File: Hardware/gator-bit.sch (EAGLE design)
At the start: 92 parts, among them J1 GATOR, J10 GATOR, J11 GATOR, J12 GATOR, J13 GATOR, J14 GATOR, J15 GATOR, J16 GATOR, J17 GATOR, J18 GATOR, J2 GATOR, J3 GATOR, J4 GATOR, J6 GATOR, J7 GATOR, J8 GATOR, J9 GATOR, U1 TPS63070, U2 micro:bit, U3 TXB0104, U4 ADJ REG 1.5A

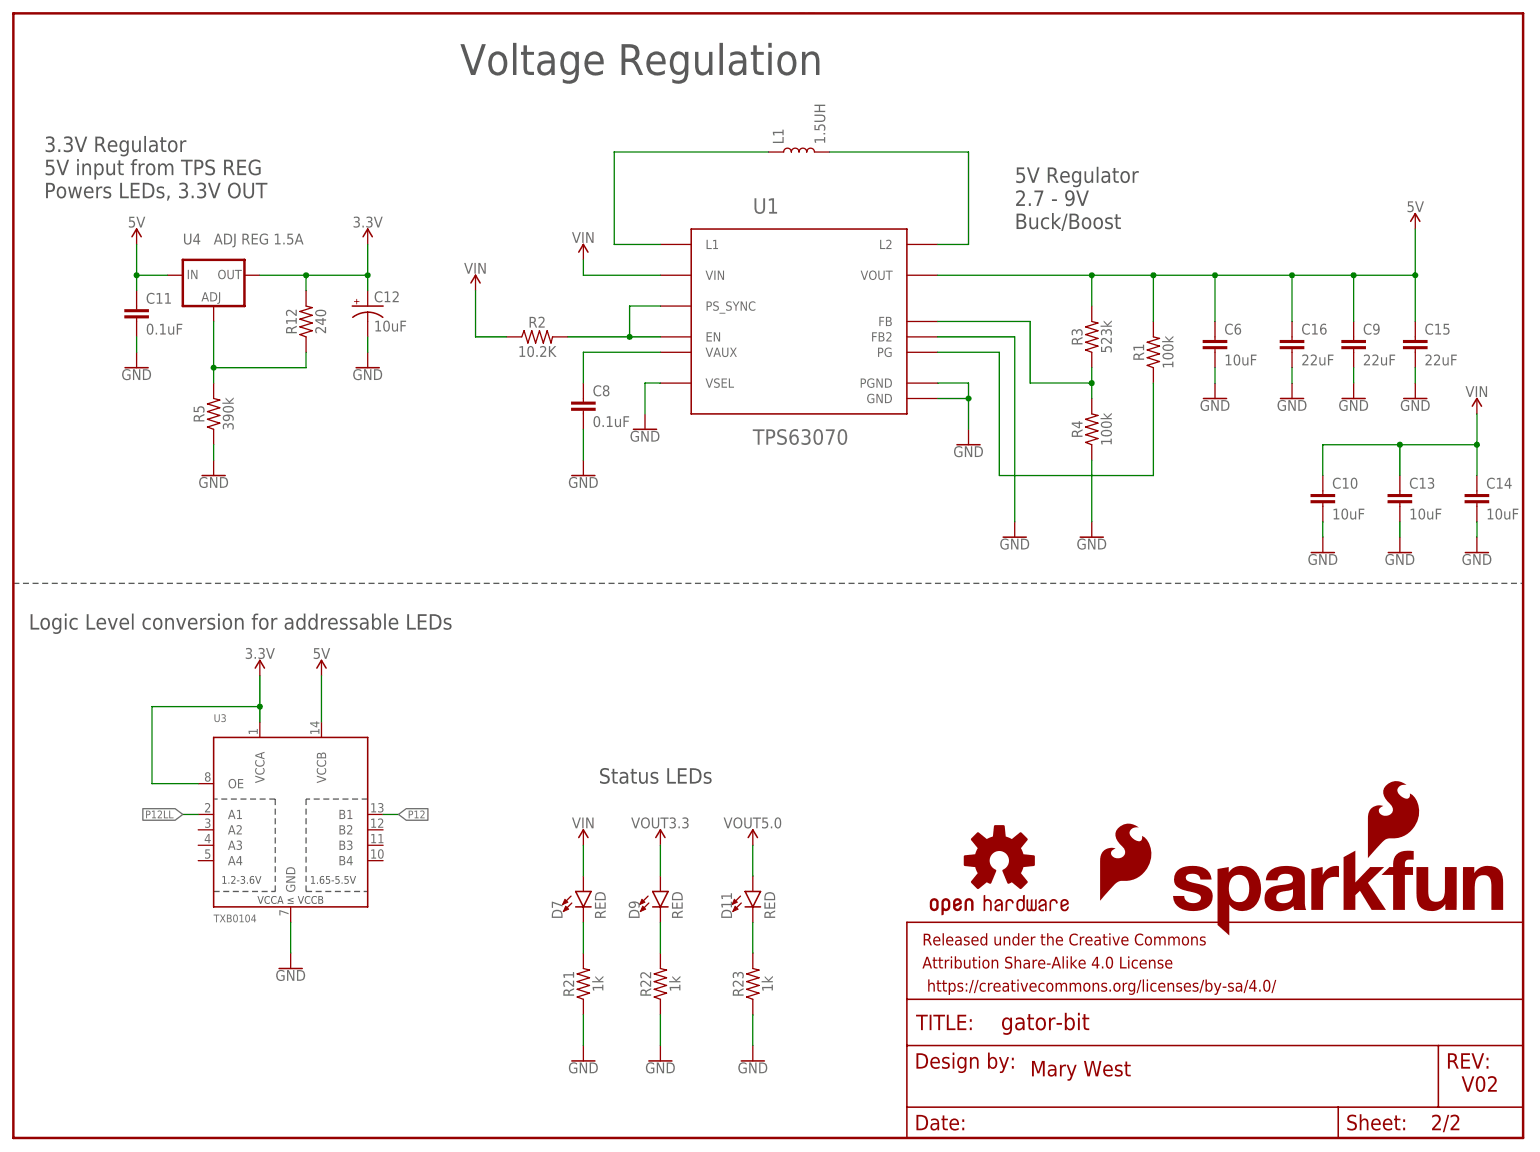
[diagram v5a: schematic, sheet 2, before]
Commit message: Updating TXB package
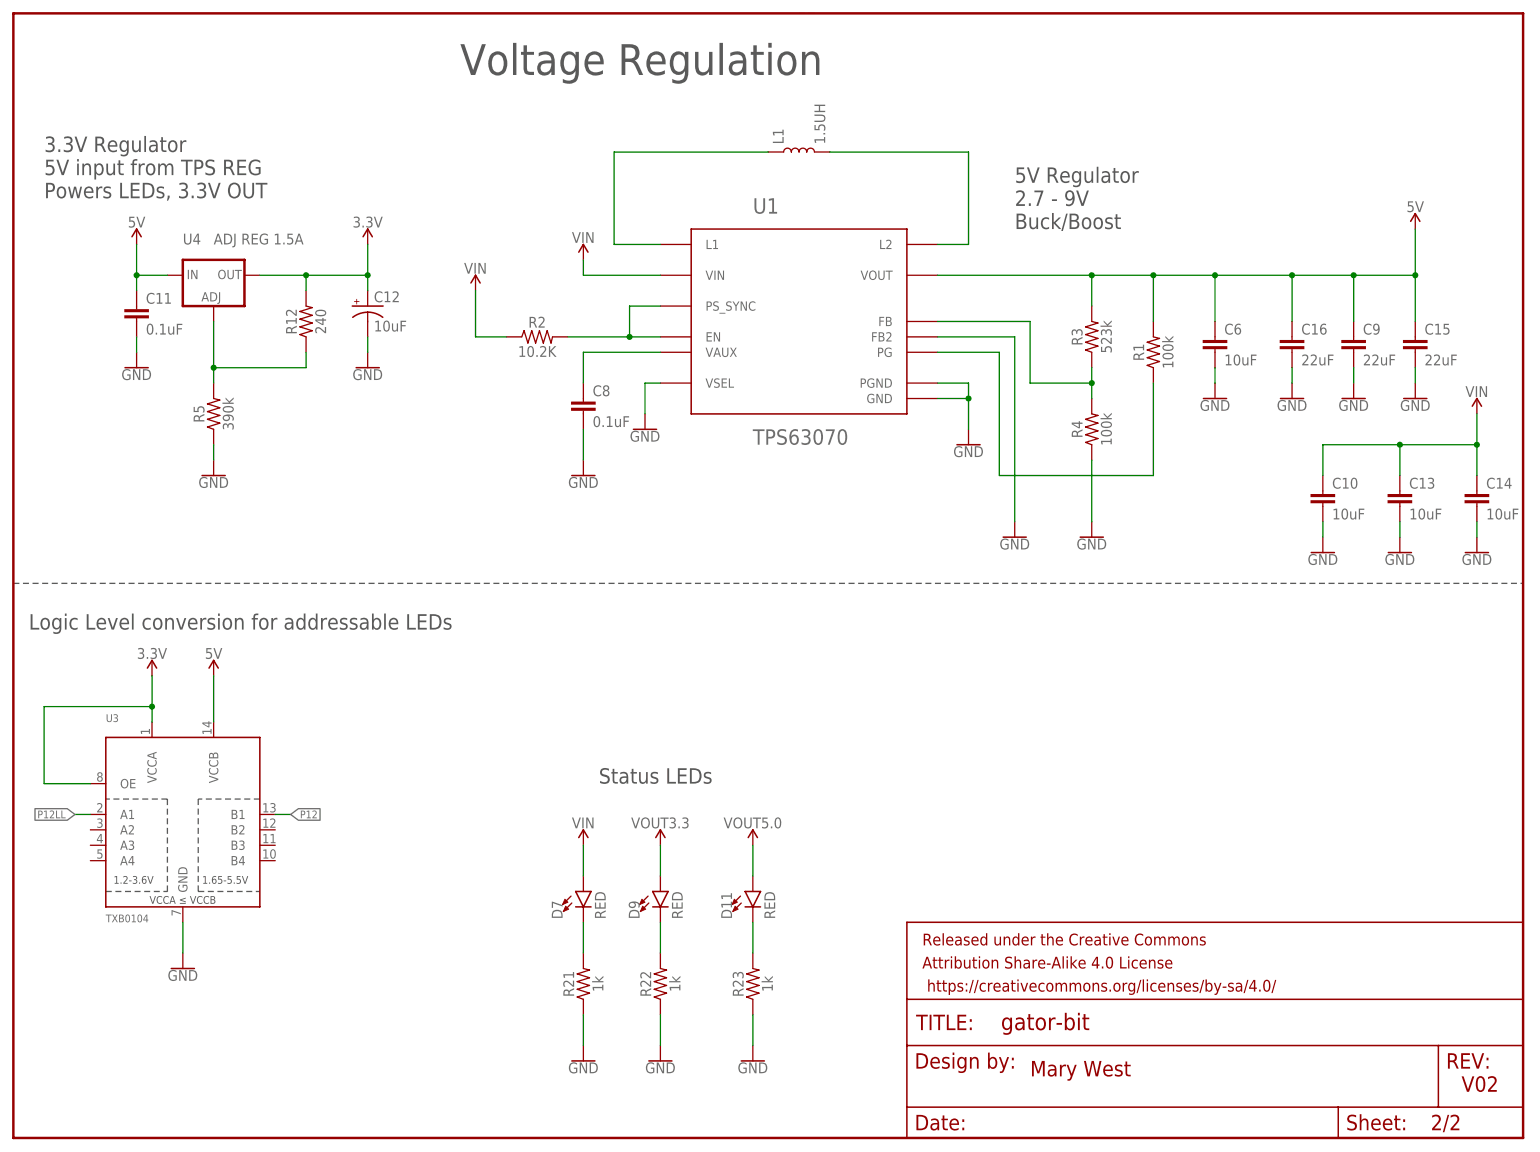
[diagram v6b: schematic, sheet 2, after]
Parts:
- removed LOGO4: SFE_LOGO_NAME_FLAME.3_INCH, SparkFun-Aesthetics:SFE_LOGO_NAME_FLAME.3_INCH
- removed LOGO5: SFE_LOGO_FLAME.3_INCH, SparkFun-Aesthetics:SFE_LOGO_FLAME.3_INCH
- removed LOGO6: OSHW-LOGOL, SparkFun-Aesthetics:OSHW-LOGOL
- added LOGO1: SFE_LOGO_NAME_FLAME.3_INCH, SparkFun-Aesthetics:SFE_LOGO_NAME_FLAME.3_INCH
- added LOGO2: OSHW-LOGOM, SparkFun-Aesthetics:OSHW-LOGOM
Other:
- moved on the sheet: U3
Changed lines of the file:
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@@
 <?xml version="1.0" encoding="utf-8"?>
 <!DOCTYPE eagle SYSTEM "eagle.dtd">
-<eagle version="8.5.1">
+<eagle version="7.7.0">
 <drawing>
 <settings>
 <setting alwaysvectorfont="no"/>
-<setting keepoldvectorfont="yes"/>
 <setting verticaltext="up"/>
 </settings>
@@
 <part name="S2" library="SparkFun-Switches" deviceset="SWITCH-SPDT" device="-SMD-AYZ0202"/>
 <part name="D6" library="SparkFun-DiscreteSemi" deviceset="DIODE-SCHOTTKY" device="-BAT20J" value="1A/23V/620mV"/>
-<part name="LOGO4" library="SparkFun-Aesthetics" deviceset="SFE_LOGO_NAME_FLAME" device=".3_INCH"/>
-<part name="LOGO5" library="SparkFun-Aesthetics" deviceset="SFE_LOGO_FLAME" device=".3_INCH" value="SFE_LOGO_FLAME.3_INCH"/>
-<part name="LOGO6" library="SparkFun-Aesthetics" deviceset="OSHW-LOGO" device="L"/>
 <part name="SUPPLY1" library="SparkFun-PowerSymbols" deviceset="5V" device=""/>
 <part name="C10" library="SparkFun-Capacitors" deviceset="10UF" device="-0805-10V-10%" value="10uF"/>
@@
 <part name="F1" library="SparkFun-Fuses" deviceset="PPTC" device="_HALF-AMP" value="6V/0.5A"/>
 <part name="SUPPLY3" library="SparkFun-PowerSymbols" deviceset="3.3V" device=""/>
+<part name="LOGO1" library="SparkFun-Aesthetics" deviceset="SFE_LOGO_NAME_FLAME" device=".3_INCH" value="SFE_LOGO_NAME_FLAME.3_INCH"/>
+<part name="LOGO2" library="SparkFun-Aesthetics" deviceset="OSHW-LOGO" device="M" value="OSHW-LOGOM"/>
 </parts>
 <sheets>
@@
 </instance>
 <instance part="SUPPLY3" gate="G$1" x="68.58" y="172.72"/>
+<instance part="LOGO1" gate="G$1" x="193.04" y="33.02"/>
+<instance part="LOGO2" gate="G$1" x="172.72" y="45.72"/>
 </instances>
 <busses>
@@
 <instance part="R12" gate="G$1" x="48.26" y="134.62" rot="R90"/>
 <instance part="GND28" gate="1" x="33.02" y="109.22"/>
-<instance part="LOGO4" gate="G$1" x="190.5" y="33.02"/>
-<instance part="LOGO5" gate="G$1" x="178.816" y="38.608"/>
-<instance part="LOGO6" gate="G$1" x="162.56" y="45.72"/>
 <instance part="C10" gate="G$1" x="215.9" y="104.14"/>
 <instance part="C13" gate="G$1" x="228.6" y="104.14"/>
@@
 <instance part="GND30" gate="1" x="215.9" y="96.52"/>
 <instance part="SUPPLY5" gate="G$1" x="241.3" y="119.38"/>
-<instance part="U3" gate="G$1" x="45.72" y="50.8"/>
-<instance part="SUPPLY7" gate="G$1" x="40.64" y="76.2"/>
-<instance part="SUPPLY8" gate="G$1" x="50.8" y="76.2"/>
-<instance part="GND31" gate="1" x="45.72" y="27.94"/>
+<instance part="U3" gate="G$1" x="27.94" y="50.8"/>
+<instance part="SUPPLY7" gate="G$1" x="22.86" y="76.2"/>
+<instance part="SUPPLY8" gate="G$1" x="33.02" y="76.2"/>
+<instance part="GND31" gate="1" x="27.94" y="27.94"/>
 <instance part="D7" gate="G$1" x="93.98" y="40.64"/>
 <instance part="D9" gate="G$1" x="106.68" y="40.64"/>
@@
 <segment>
 <pinref part="U3" gate="G$1" pin="GND"/>
-<wire x1="45.72" y1="35.56" x2="45.72" y2="30.48" width="0.1524" layer="91"/>
+<wire x1="27.94" y1="35.56" x2="27.94" y2="30.48" width="0.1524" layer="91"/>
 <pinref part="GND31" gate="1" pin="GND"/>
 </segment>
@@
 <segment>
 <pinref part="U3" gate="G$1" pin="VCCB"/>
-<wire x1="50.8" y1="68.58" x2="50.8" y2="76.2" width="0.1524" layer="91"/>
+<wire x1="33.02" y1="68.58" x2="33.02" y2="76.2" width="0.1524" layer="91"/>
 <pinref part="SUPPLY8" gate="G$1" pin="5V"/>
 </segment>
@@
 <segment>
 <pinref part="U3" gate="G$1" pin="VCCA"/>
-<wire x1="40.64" y1="68.58" x2="40.64" y2="71.12" width="0.1524" layer="91"/>
+<wire x1="22.86" y1="68.58" x2="22.86" y2="71.12" width="0.1524" layer="91"/>
 <pinref part="SUPPLY7" gate="G$1" pin="3.3V"/>
 <pinref part="U3" gate="G$1" pin="OE"/>
-<wire x1="40.64" y1="71.12" x2="40.64" y2="76.2" width="0.1524" layer="91"/>
-<wire x1="30.48" y1="58.42" x2="22.86" y2="58.42" width="0.1524" layer="91"/>
-<wire x1="22.86" y1="58.42" x2="22.86" y2="71.12" width="0.1524" layer="91"/>
-<wire x1="22.86" y1="71.12" x2="40.64" y2="71.12" width="0.1524" layer="91"/>
-<junction x="40.64" y="71.12"/>
+<wire x1="22.86" y1="71.12" x2="22.86" y2="76.2" width="0.1524" layer="91"/>
+<wire x1="12.7" y1="58.42" x2="5.08" y2="58.42" width="0.1524" layer="91"/>
+<wire x1="5.08" y1="58.42" x2="5.08" y2="71.12" width="0.1524" layer="91"/>
+<wire x1="5.08" y1="71.12" x2="22.86" y2="71.12" width="0.1524" layer="91"/>
+<junction x="22.86" y="71.12"/>
 </segment>
 </net>
@@
 <segment>
 <pinref part="U3" gate="G$1" pin="A1"/>
-<wire x1="30.48" y1="53.34" x2="27.94" y2="53.34" width="0.1524" layer="91"/>
-<label x="27.94" y="53.34" size="1.27" layer="95" rot="R180" xref="yes"/>
+<wire x1="12.7" y1="53.34" x2="10.16" y2="53.34" width="0.1524" layer="91"/>
+<label x="10.16" y="53.34" size="1.27" layer="95" rot="R180" xref="yes"/>
 </segment>
 </net>
@@
 <segment>
 <pinref part="U3" gate="G$1" pin="B1"/>
-<wire x1="60.96" y1="53.34" x2="63.5" y2="53.34" width="0.1524" layer="91"/>
-<label x="63.5" y="53.34" size="1.27" layer="95" xref="yes"/>
-</segment>
-</net>
+<wire x1="43.18" y1="53.34" x2="45.72" y2="53.34" width="0.1524" layer="91"/>
+<label x="45.72" y="53.34" size="1.27" layer="95" xref="yes"/>
+</segment>
+</net>
